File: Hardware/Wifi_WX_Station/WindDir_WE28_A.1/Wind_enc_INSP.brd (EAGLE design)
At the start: 25.4 x 25.3 mm, 12 parts, among them IC1 EM3242, IC2 TLV2211, IC3 TC10553.3V, X1 1751251

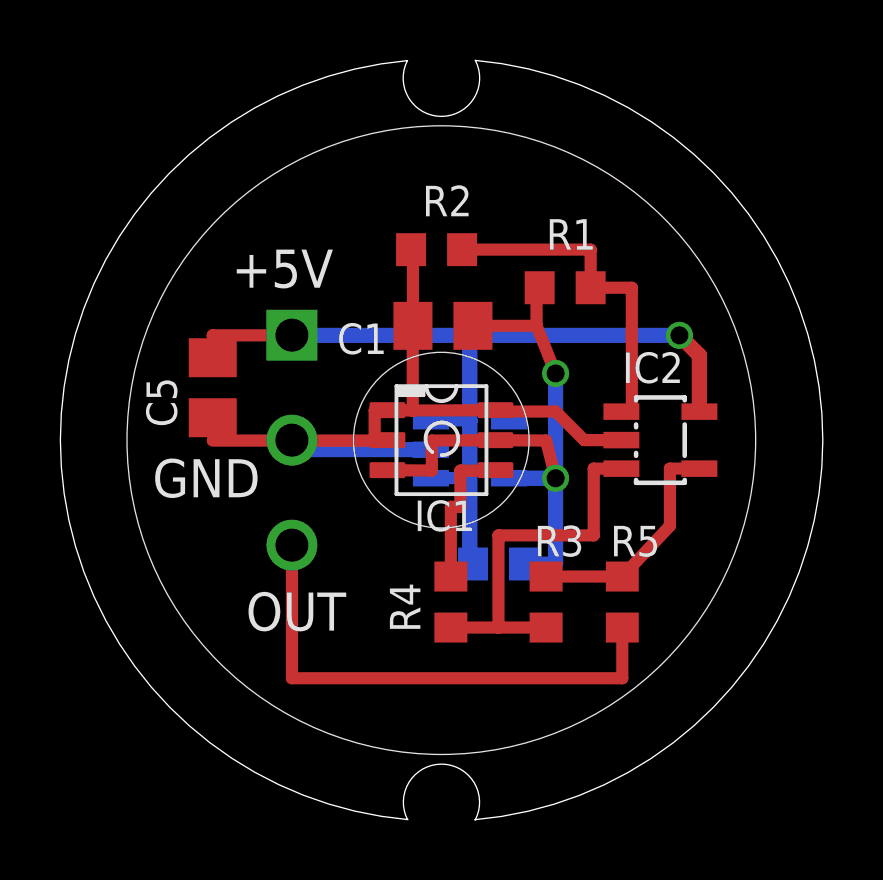
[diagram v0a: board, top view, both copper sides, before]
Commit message: added PCB for BOSH PMP180 revised WE28 schemaitc with added text
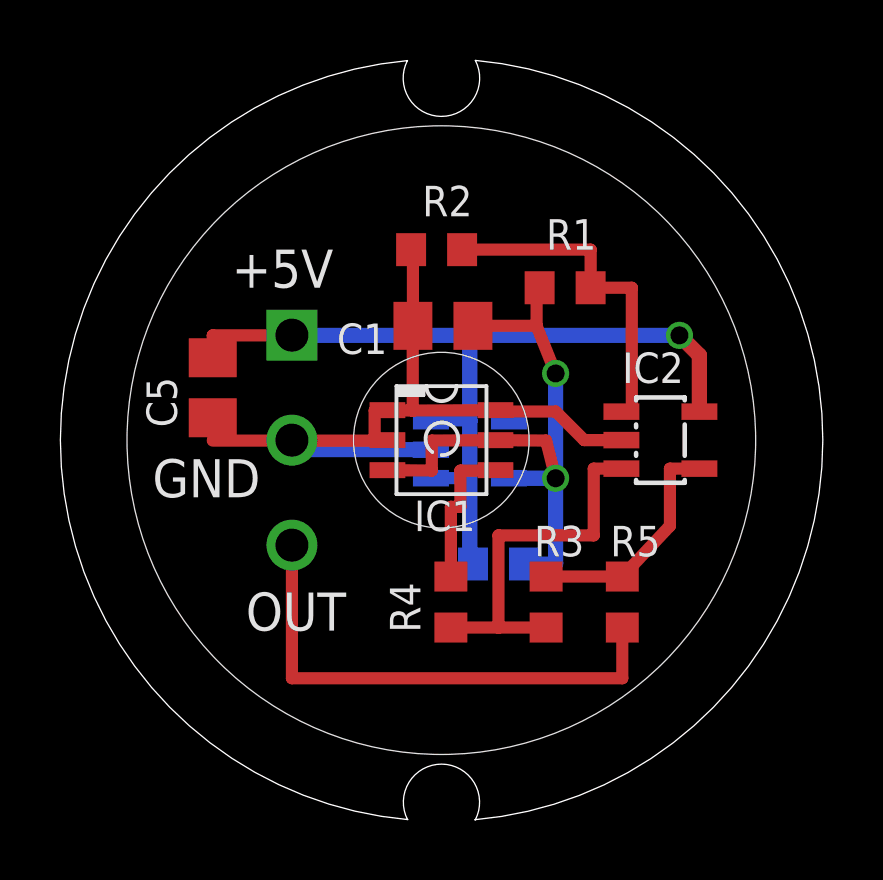
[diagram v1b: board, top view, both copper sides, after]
